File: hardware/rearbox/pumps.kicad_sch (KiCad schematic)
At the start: 25 parts, among them Q5 BUK6D210, U8 VND7020AJTR

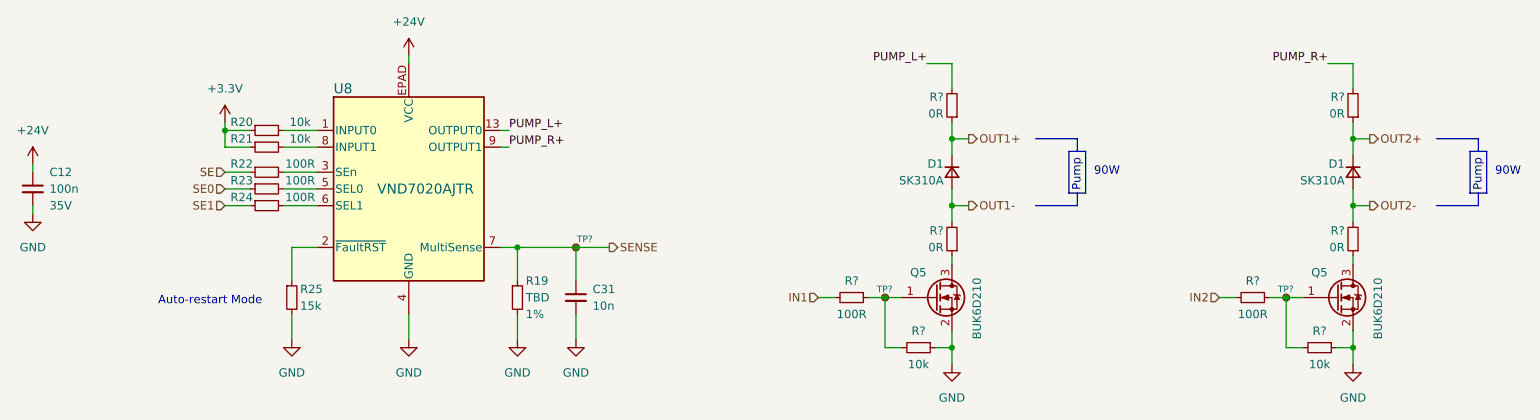
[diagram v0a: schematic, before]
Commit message: Place components on the PCB
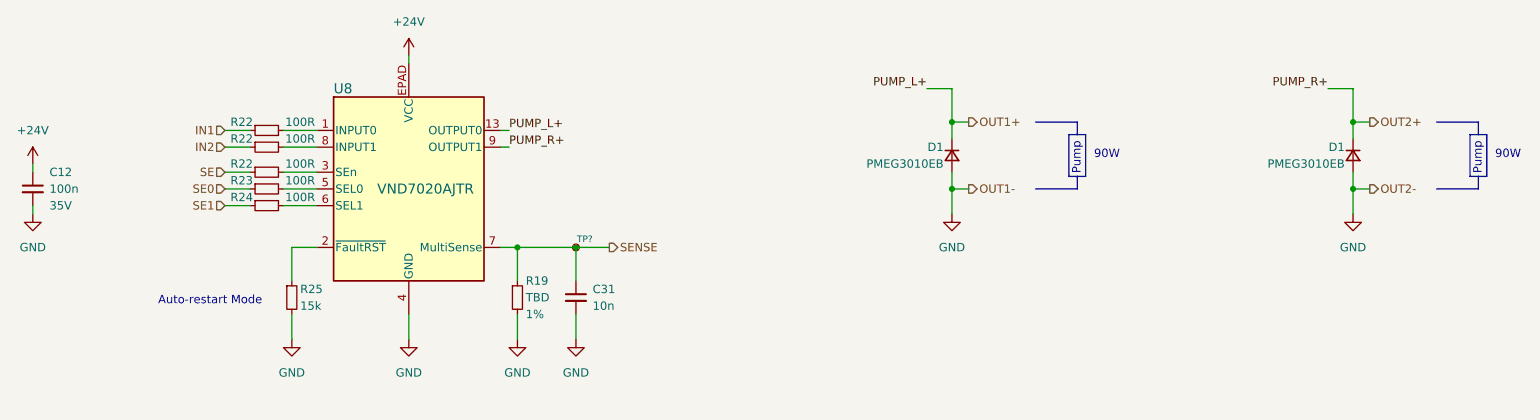
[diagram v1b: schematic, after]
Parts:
- removed Q5 (x2): BUK6D210, Package_DFN_QFN:Diodes_UDFN2020-6_Type-F, symbol Device:Q_NMOS_GSD
- removed R20, R21, R? (x2): 10k, Resistor_SMD:R_0603_1608Metric, symbol Device:R_Small
- removed R? (x4): 0R, Resistor_SMD:R_0603_1608Metric, symbol Device:R_Small
- removed R? (x2): 100R, Resistor_SMD:R_0603_1608Metric, symbol Device:R_Small
- removed TP? (x2): TestPoint_Small, TestPoint:TestPoint_Pad_D1.0mm, symbol Connector:TestPoint_Small
- added R22 (x2): 100R, Resistor_SMD:R_0603_1608Metric, symbol Device:R_Small
- C12: footprint Capacitor_SMD:C_0603_1608Metric -> Capacitor_SMD:C_0805_2012Metric
- D1: value SK310A -> PMEG3010EB; footprint Diode_SMD:D_SMA -> Diode_SMD:D_SOD-523
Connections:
- net OUT1- is gone; now on net GND: D1.2 (A)
- net OUT2- is gone; now on net GND: D1.2 (A)
- net PUMP_L+ is gone; now on net OUT1+: U8.13 (OUTPUT0), U8.14 (OUTPUT0), U8.15 (OUTPUT0), U8.16 (OUTPUT0)
- net PUMP_R+ is gone; now on net OUT2+: U8.10 (OUTPUT1), U8.11 (OUTPUT1), U8.12 (OUTPUT1), U8.9 (OUTPUT1)
- net IN1: now also R22.1
- net IN2: now also R22.1
- net at U8.8 (INPUT1): now also R22.2
- net at U8.1 (INPUT0): now also R22.2
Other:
- moved on the sheet: D1
